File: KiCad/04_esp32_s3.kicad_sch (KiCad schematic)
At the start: 35 parts, among them IC401 ESP32-S3-WROOM-1-N16R8, J1 Conn_01x08_Pin, J401 Conn_01x04_Pin, J403 Conn_01x04_Pin, J404 TF-01A, Q401 SS8050, Q402 SS8050

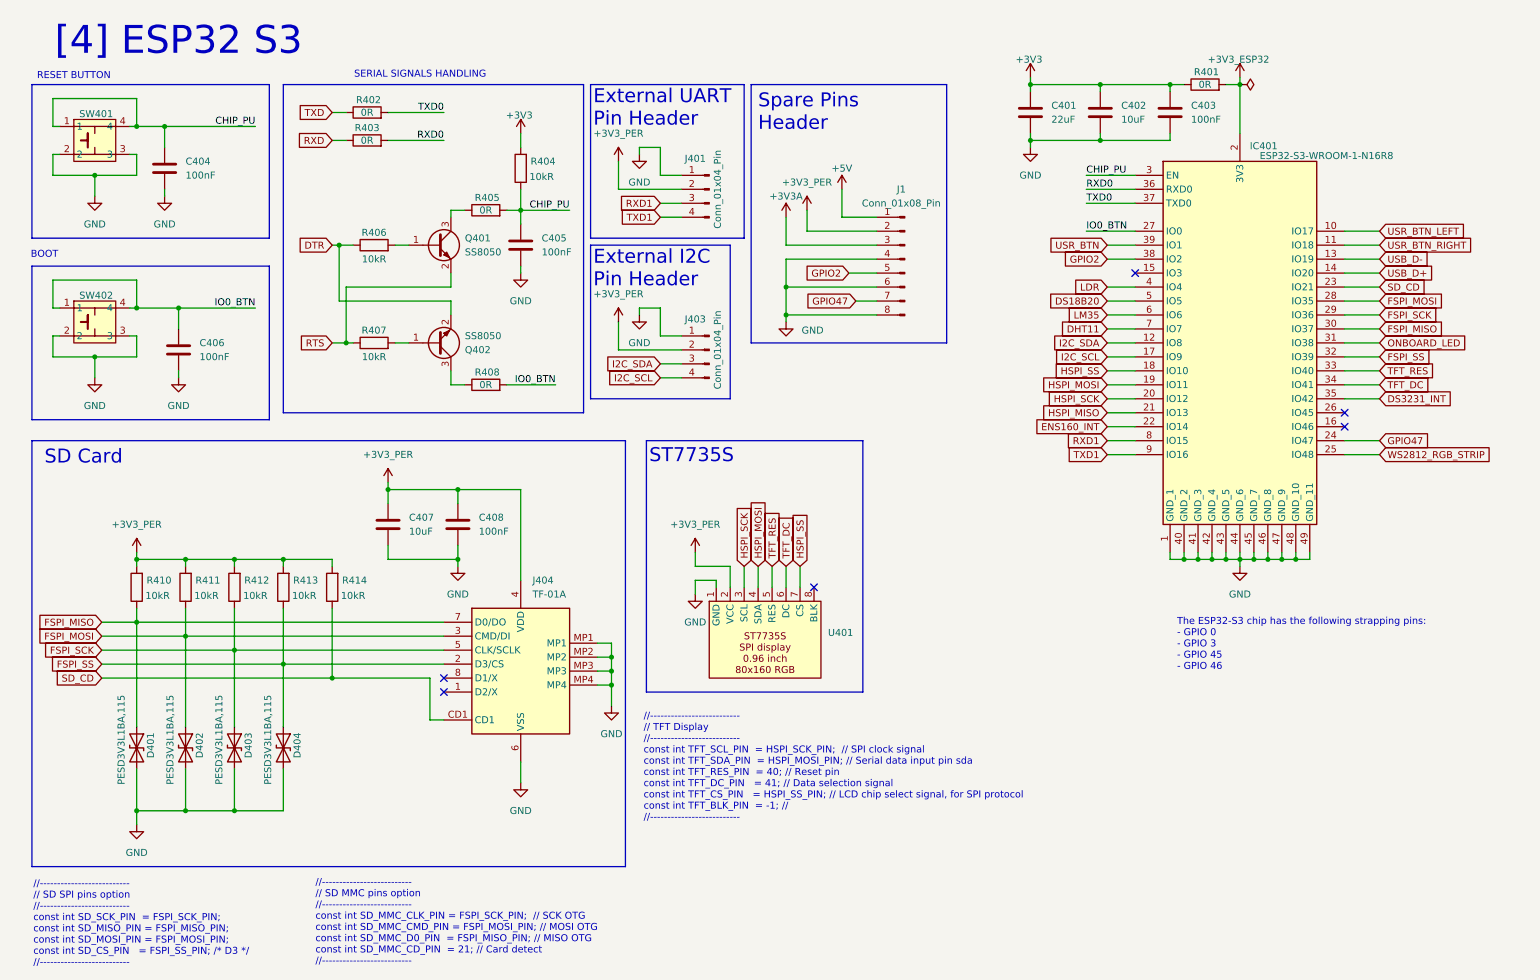
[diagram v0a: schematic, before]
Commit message: Add UART pin header
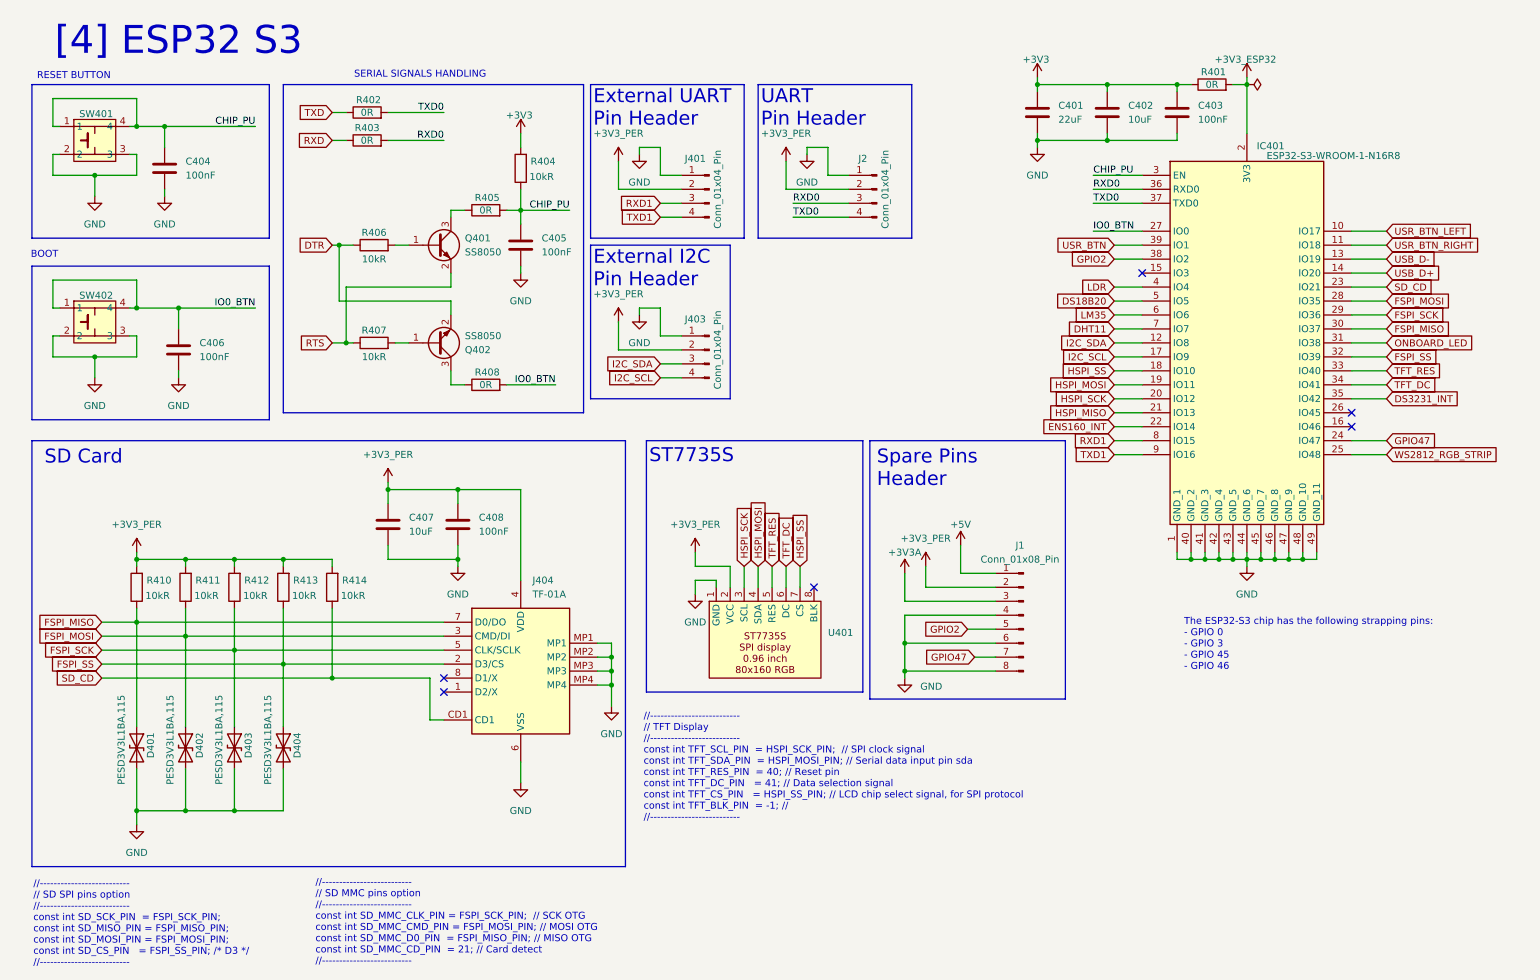
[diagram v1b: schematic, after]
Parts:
- added J2: Conn_01x04_Pin, Connector_PinHeader_2.54mm:PinHeader_1x04_P2.54mm_Vertical, symbol Connector:Conn_01x04_Pin
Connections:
- net +3V3_PER: now also J2.2 (Pin_2)
- net GND: now also J2.1 (Pin_1)
- net RXD0: now also J2.3 (Pin_3)
- net TXD0: now also J2.4 (Pin_4)
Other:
- note added: "UART Pin Header"
- moved on the sheet: C401, C402, C403, IC401, J1, R401

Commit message: Add sensor footprints
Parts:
- U401: footprint (none) -> esp32_s3_weather_webserver:ST7735S
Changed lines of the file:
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@@
 			)
 		)
-		(property "Footprint" ""
+		(property "Footprint" "esp32_s3_weather_webserver:ST7735S"
 			(at 139.7 123.19 0)
 			(effects

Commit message: BOM updates
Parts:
- C408: Manufacturer Part Number CL10B104KA8NNNC -> CL10B104KB8NNNC
- IC401: Manufacturer (none) -> ESPRESSIF; Manufacturer Part Number (none) -> ESP32-S3-WROOM-1-N16R8
- J1: footprint (none) -> Connector_PinHeader_2.54mm:PinHeader_1x08_P2.54mm_Vertical
- J404: Manufacturer (none) -> Korean Hroparts Elec; Manufacturer Part Number (none) -> TF-01A
- Q401, Q402: Manufacturer (none) -> JSMSEMI; Manufacturer Part Number (none) -> SS8050
- SW401, SW402: Manufacturer (none) -> SM Switch; Manufacturer Part Number (none) -> SMG-01-H080A1
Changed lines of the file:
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@@
 			)
 		)
+		(property "Manufacturer" "JSMSEMI"
+			(at 90.17 58.42 0)
+			(effects
+				(font
+					(size 1.27 1.27)
+				)
+				(hide yes)
+			)
+		)
+		(property "Manufacturer Part Number" "SS8050"
+			(at 90.17 58.42 0)
+			(effects
+				(font
+					(size 1.27 1.27)
+				)
+				(hide yes)
+			)
+		)
 		(pin "3"
 		)
@@
 			)
 		)
+		(property "Manufacturer" "SM Switch"
+			(at 27.94 71.12 0)
+			(effects
+				(font
+					(size 1.27 1.27)
+				)
+				(hide yes)
+			)
+		)
+		(property "Manufacturer Part Number" "SMG-01-H080A1"
+			(at 27.94 71.12 0)
+			(effects
+				(font
+					(size 1.27 1.27)
+				)
+				(hide yes)
+			)
+		)
 		(pin "2"
 		)
@@
 			)
 		)
+		(property "Manufacturer" "Korean Hroparts Elec"
+			(at 96.52 124.46 0)
+			(effects
+				(font
+					(size 1.27 1.27)
+				)
+				(hide yes)
+			)
+		)
+		(property "Manufacturer Part Number" "TF-01A"
+			(at 96.52 124.46 0)
+			(effects
+				(font
+					(size 1.27 1.27)
+				)
+				(hide yes)
+			)
+		)
 		(pin "MP4"
 		)
@@
 			)
 		)
+		(property "Manufacturer" "SM Switch"
+			(at 27.94 38.1 0)
+			(effects
+				(font
+					(size 1.27 1.27)
+				)
+				(hide yes)
+			)
+		)
+		(property "Manufacturer Part Number" "SMG-01-H080A1"
+			(at 27.94 38.1 0)
+			(effects
+				(font
+					(size 1.27 1.27)
+				)
+				(hide yes)
+			)
+		)
 		(pin "2"
 		)
@@
 			)
 		)
-		(property "Footprint" ""
+		(property "Footprint" "Connector_PinHeader_2.54mm:PinHeader_1x08_P2.54mm_Vertical"
 			(at 196.85 125.73 0)
 			(effects
@@
 			)
 		)
+		(property "Manufacturer" "ESPRESSIF"
+			(at 223.52 43.18 0)
+			(effects
+				(font
+					(size 1.27 1.27)
+				)
+				(hide yes)
+			)
+		)
+		(property "Manufacturer Part Number" "ESP32-S3-WROOM-1-N16R8"
+			(at 223.52 43.18 0)
+			(effects
+				(font
+					(size 1.27 1.27)
+				)
+				(hide yes)
+			)
+		)
 		(pin "33"
 		)
@@
 			)
 		)
+		(property "Manufacturer" "JSMSEMI"
+			(at 90.17 76.2 0)
+			(effects
+				(font
+					(size 1.27 1.27)
+				)
+				(hide yes)
+			)
+		)
+		(property "Manufacturer Part Number" "SS8050"
+			(at 90.17 76.2 0)
+			(effects
+				(font
+					(size 1.27 1.27)
+				)
+				(hide yes)
+			)
+		)
 		(pin "3"
 		)
@@
 			)
 		)
-		(property "Manufacturer Part Number" "CL10B104KA8NNNC"
+		(property "Manufacturer Part Number" "CL10B104KB8NNNC"
 			(at 93.98 109.22 0)
 			(effects

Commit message: BOM updates. First layout
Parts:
- C403, C404, C405, C406, C408: footprint Capacitor_SMD:C_0603_1608Metric -> Capacitor_SMD:C_0402_1005Metric; Manufacturer Part Number CL10B104KB8NNNC -> CL05B104KO5NNNC
- R404, R406, R407: footprint Resistor_SMD:R_0805_2012Metric -> Resistor_SMD:R_0402_1005Metric
- R409: renamed from R410; footprint Resistor_SMD:R_0805_2012Metric -> Resistor_SMD:R_0402_1005Metric
- R410: renamed from R411; footprint Resistor_SMD:R_0805_2012Metric -> Resistor_SMD:R_0402_1005Metric
- R411: renamed from R412; footprint Resistor_SMD:R_0805_2012Metric -> Resistor_SMD:R_0402_1005Metric
- R412: renamed from R413; footprint Resistor_SMD:R_0805_2012Metric -> Resistor_SMD:R_0402_1005Metric
- R413: renamed from R414; footprint Resistor_SMD:R_0805_2012Metric -> Resistor_SMD:R_0402_1005Metric
- renumbered J2 to J402, J1 to J405
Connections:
- net +3V3A is gone; now on net +3V3_PER: J405.3 (Pin_3)
- net +3V3: now also J405.2 (Pin_2)
- net +3V3_PER: no longer J405.2 (Pin_2)

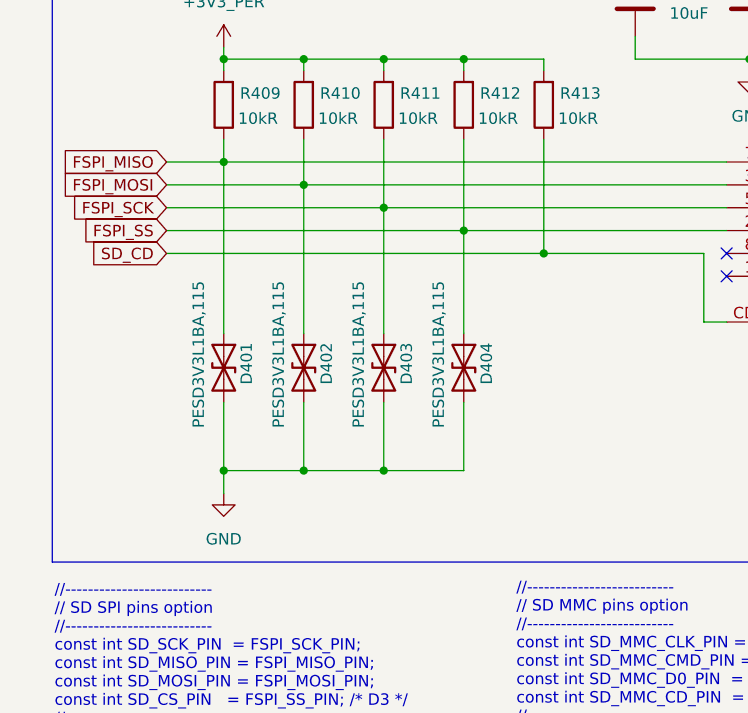
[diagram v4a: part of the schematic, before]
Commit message: PCB layout updates
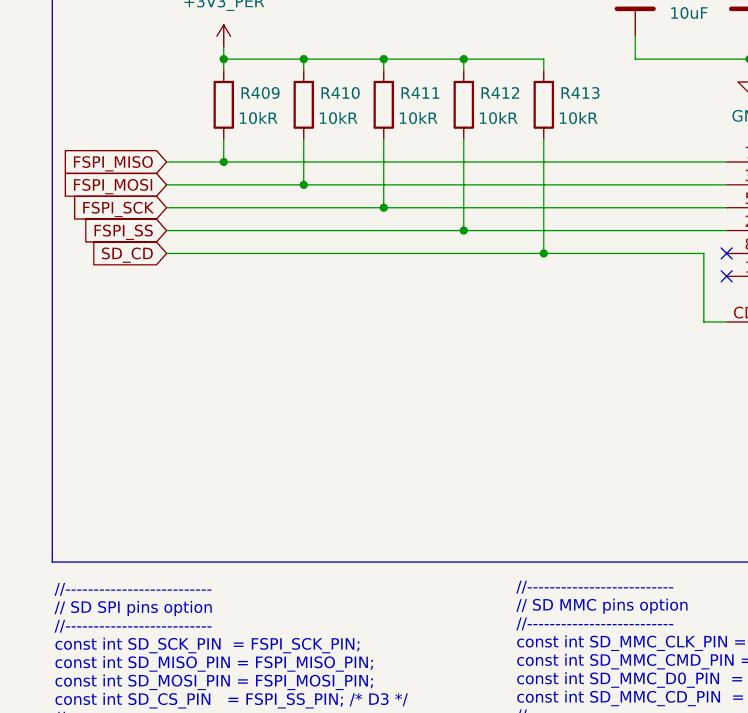
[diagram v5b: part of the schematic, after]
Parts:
- removed D401, D402, D403, D404: PESD3V3L1BA,115, Diode_SMD:D_SOD-323, symbol Device:D_TVS

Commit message: Simple routing
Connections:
- net +3V3: now also J401.2 (Pin_2), J402.2 (Pin_2)
- net +3V3_PER: no longer J401.2 (Pin_2), J402.2 (Pin_2)
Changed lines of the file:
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@@
 	)
 	(symbol
-		(lib_id "power:+3.3V")
-		(at 153.67 43.18 0)
-		(unit 1)
-		(exclude_from_sim no)
-		(in_bom yes)
-		(on_board yes)
-		(dnp no)
-		(fields_autoplaced yes)
-		(property "Reference" "#PWR0408"
-			(at 153.67 46.99 0)
-			(effects
-				(font
-					(size 1.27 1.27)
-				)
-				(hide yes)
-			)
-		)
-		(property "Value" "+3V3_PER"
-			(at 153.67 38.1 0)
-			(effects
-				(font
-					(size 1.27 1.27)
-				)
-			)
-		)
-		(property "Footprint" ""
-			(at 153.67 43.18 0)
-			(effects
-				(font
-					(size 1.27 1.27)
-				)
-				(hide yes)
-			)
-		)
-		(property "Datasheet" ""
-			(at 153.67 43.18 0)
-			(effects
-				(font
-					(size 1.27 1.27)
-				)
-				(hide yes)
-			)
-		)
-		(property "Description" "Power symbol creates a global label with name \"+3.3V\""
-			(at 153.67 43.18 0)
-			(effects
-				(font
-					(size 1.27 1.27)
-				)
-				(hide yes)
-			)
-		)
-		(pin "1"
-		)
-		(instances
-			(project "esp32_s3_weather_webserver"
-				(path "/04e96486-ec4c-4881-a0bf-37cb6ce91c2d/50304ef4-c32e-4a1f-a652-b7b630d07cc6"
-					(reference "#PWR0408")
-					(unit 1)
-				)
-			)
-		)
-	)
-	(symbol
 		(lib_id "Connector:Conn_01x08_Pin")
 		(at 196.85 125.73 0)
@@
 	)
 	(symbol
+		(lib_id "power:+3.3V")
+		(at 123.19 43.18 0)
+		(unit 1)
+		(exclude_from_sim no)
+		(in_bom yes)
+		(on_board yes)
+		(dnp no)
+		(property "Reference" "#PWR05"
+			(at 123.19 46.99 0)
+			(effects
+				(font
+					(size 1.27 1.27)
+				)
+				(hide yes)
+			)
+		)
+		(property "Value" "+3V3"
+			(at 122.936 39.878 0)
+			(effects
+				(font
+					(size 1.27 1.27)
+				)
+			)
+		)
+		(property "Footprint" ""
+			(at 123.19 43.18 0)
+			(effects
+				(font
+					(size 1.27 1.27)
+				)
+				(hide yes)
+			)
+		)
+		(property "Datasheet" ""
+			(at 123.19 43.18 0)
+			(effects
+				(font
+					(size 1.27 1.27)
+				)
+				(hide yes)
+			)
+		)
+		(property "Description" "Power symbol creates a global label with name \"+3.3V\""
+			(at 123.19 43.18 0)
+			(effects
+				(font
+					(size 1.27 1.27)
+				)
+				(hide yes)
+			)
+		)
+		(pin "1"
+		)
+		(instances
+			(project "esp32_s3_weather_webserver"
+				(path "/04e96486-ec4c-4881-a0bf-37cb6ce91c2d/50304ef4-c32e-4a1f-a652-b7b630d07cc6"
+					(reference "#PWR05")
+					(unit 1)
+				)
+			)
+		)
+	)
+	(symbol
 		(lib_name "GND_3")
 		(lib_id "power:GND")
@@
 	)
 	(symbol
-		(lib_id "power:+3.3V")
-		(at 123.19 43.18 0)
-		(unit 1)
-		(exclude_from_sim no)
-		(in_bom yes)
-		(on_board yes)
-		(dnp no)
-		(fields_autoplaced yes)
-		(property "Reference" "#PWR0407"
-			(at 123.19 46.99 0)
-			(effects
-				(font
-					(size 1.27 1.27)
-				)
-				(hide yes)
-			)
-		)
-		(property "Value" "+3V3_PER"
-			(at 123.19 38.1 0)
-			(effects
-				(font
-					(size 1.27 1.27)
-				)
-			)
-		)
-		(property "Footprint" ""
-			(at 123.19 43.18 0)
-			(effects
-				(font
-					(size 1.27 1.27)
-				)
-				(hide yes)
-			)
-		)
-		(property "Datasheet" ""
-			(at 123.19 43.18 0)
-			(effects
-				(font
-					(size 1.27 1.27)
-				)
-				(hide yes)
-			)
-		)
-		(property "Description" "Power symbol creates a global label with name \"+3.3V\""
-			(at 123.19 43.18 0)
-			(effects
-				(font
-					(size 1.27 1.27)
-				)
-				(hide yes)
-			)
-		)
-		(pin "1"
-		)
-		(instances
-			(project "esp32_s3_weather_webserver"
-				(path "/04e96486-ec4c-4881-a0bf-37cb6ce91c2d/50304ef4-c32e-4a1f-a652-b7b630d07cc6"
-					(reference "#PWR0407")
-					(unit 1)
-				)
-			)
-		)
-	)
-	(symbol
 		(lib_id "Device:R")
 		(at 77.47 39.37 90)
@@
 					(unit 1)
 				)
+			)
+		)
+	)
+	(symbol
+		(lib_id "power:+3.3V")
+		(at 153.67 43.18 0)
+		(unit 1)
+		(exclude_from_sim no)
+		(in_bom yes)
+		(on_board yes)
+		(dnp no)
+		(property "Reference" "#PWR04"
+			(at 153.67 46.99 0)
+			(effects
+				(font
+					(size 1.27 1.27)
+				)
+				(hide yes)
+			)
+		)
+		(property "Value" "+3V3"
+			(at 153.416 39.878 0)
+			(effects
+				(font
+					(size 1.27 1.27)
+				)
+			)
+		)
+		(property "Footprint" ""
+			(at 153.67 43.18 0)
+			(effects
+				(font
+					(size 1.27 1.27)
+				)
+				(hide yes)
+			)
+		)
+		(property "Datasheet" ""
+			(at 153.67 43.18 0)
+			(effects
+				(font
+					(size 1.27 1.27)
+				)
+				(hide yes)
+			)
+		)
+		(property "Description" "Power symbol creates a global label with name \"+3.3V\""
+			(at 153.67 43.18 0)
+			(effects
+				(font
+					(size 1.27 1.27)
+				)
+				(hide yes)
+			)
+		)
+		(pin "1"
+		)
+		(instances
+			(project "esp32_s3_weather_webserver"
+				(path "/04e96486-ec4c-4881-a0bf-37cb6ce91c2d/50304ef4-c32e-4a1f-a652-b7b630d07cc6"
+					(reference "#PWR04")
+					(unit 1)
+				)

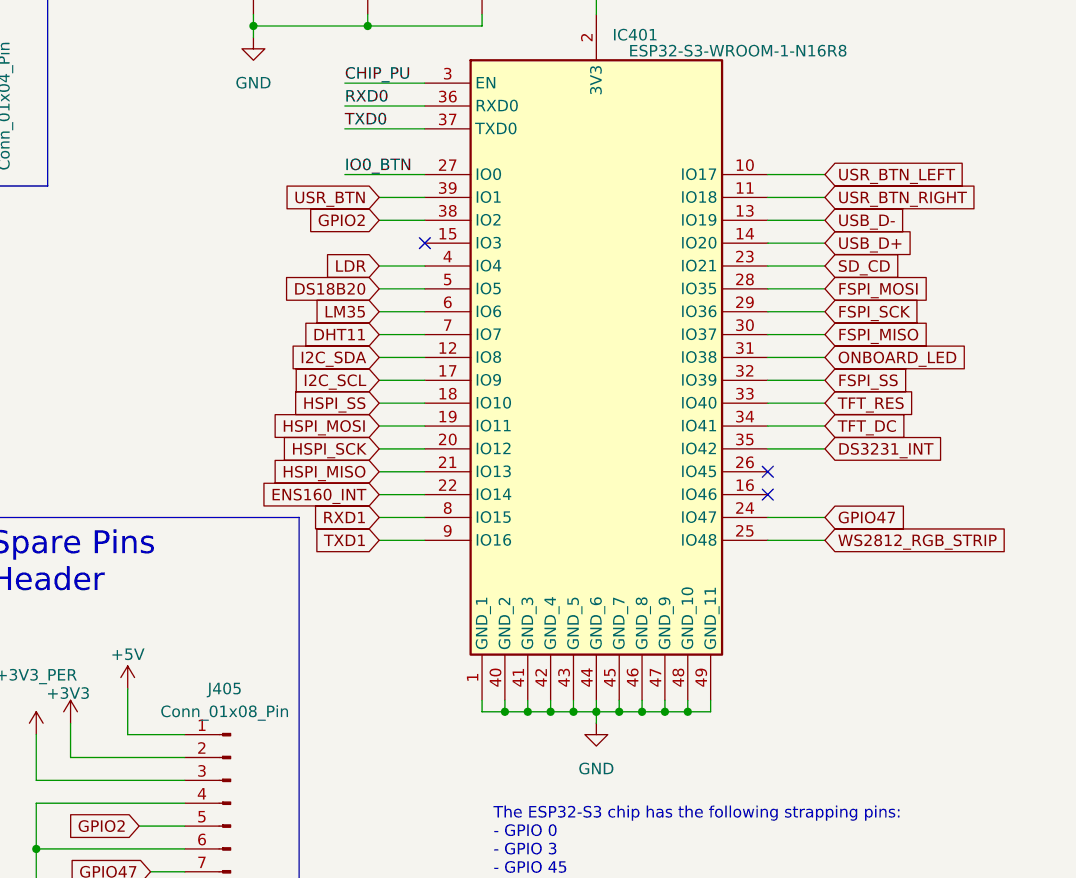
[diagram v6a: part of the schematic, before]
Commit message: SPI signals routing
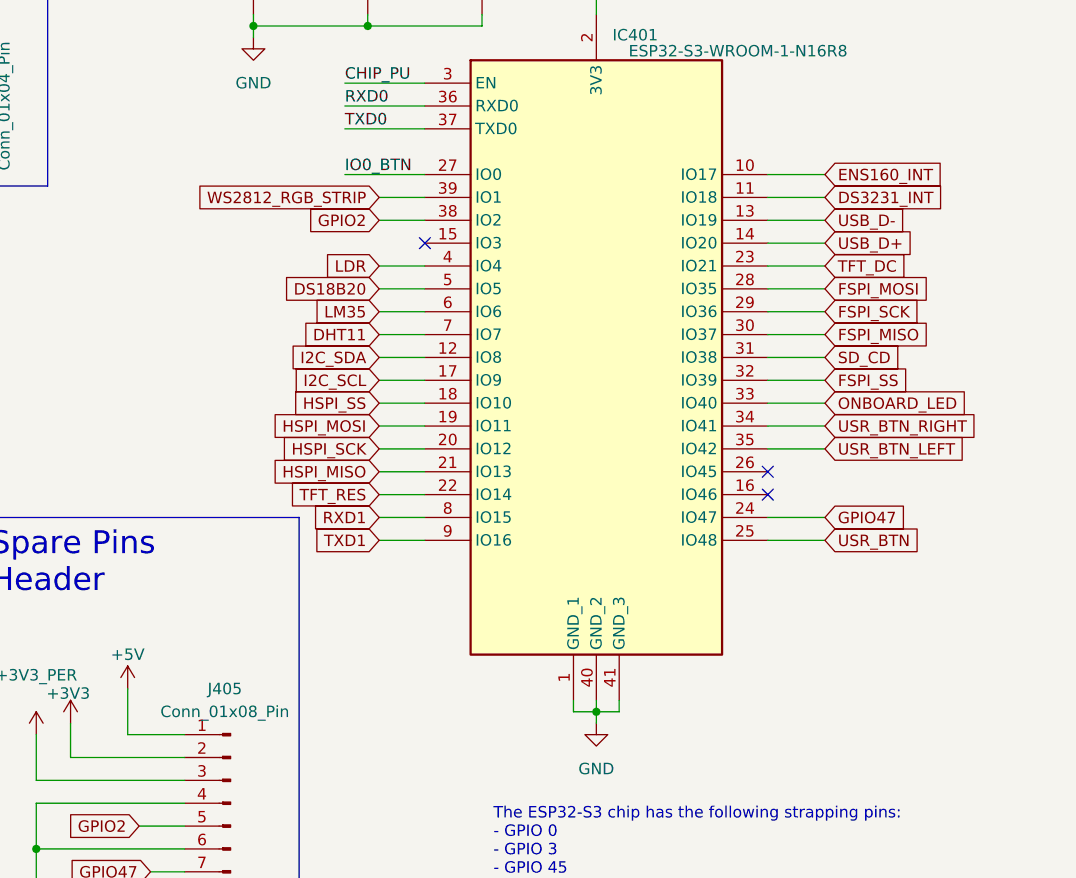
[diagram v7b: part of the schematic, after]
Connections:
- net DS3231_INT: now also IC401.11 (IO18); no longer IC401.35 (IO42)
- net ENS160_INT: now also IC401.10 (IO17); no longer IC401.22 (IO14)
- net GND: no longer IC401.42 (GND_4), IC401.43 (GND_5), IC401.44 (GND_6), IC401.45 (GND_7), IC401.46 (GND_8), IC401.47 (GND_9), IC401.48 (GND_10), IC401.49 (GND_11)
- net ONBOARD_LED: now also IC401.33 (IO40); no longer IC401.31 (IO38)
- net SD_CD: now also IC401.31 (IO38); no longer IC401.23 (IO21)
- net TFT_DC: now also IC401.23 (IO21); no longer IC401.34 (IO41)
- net TFT_RES: now also IC401.22 (IO14); no longer IC401.33 (IO40)
- net USR_BTN: now also IC401.25 (IO48); no longer IC401.39 (IO1)
- net USR_BTN_LEFT: now also IC401.35 (IO42); no longer IC401.10 (IO17)
- net USR_BTN_RIGHT: now also IC401.34 (IO41); no longer IC401.11 (IO18)
- net WS2812_RGB_STRIP: now also IC401.39 (IO1); no longer IC401.25 (IO48)
